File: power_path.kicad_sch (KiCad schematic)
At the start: 34 parts, among them J2 USB_C_Receptacle_USB2.0_16P, SW1 SW_SPST, U2 TPS631000DRLR, U3 TLV77018PDBVR, U4 TPS2116DRL, U5 USBLC6-2SC6, U6 USBLC6-2SC6, U8 BQ27427YZFR

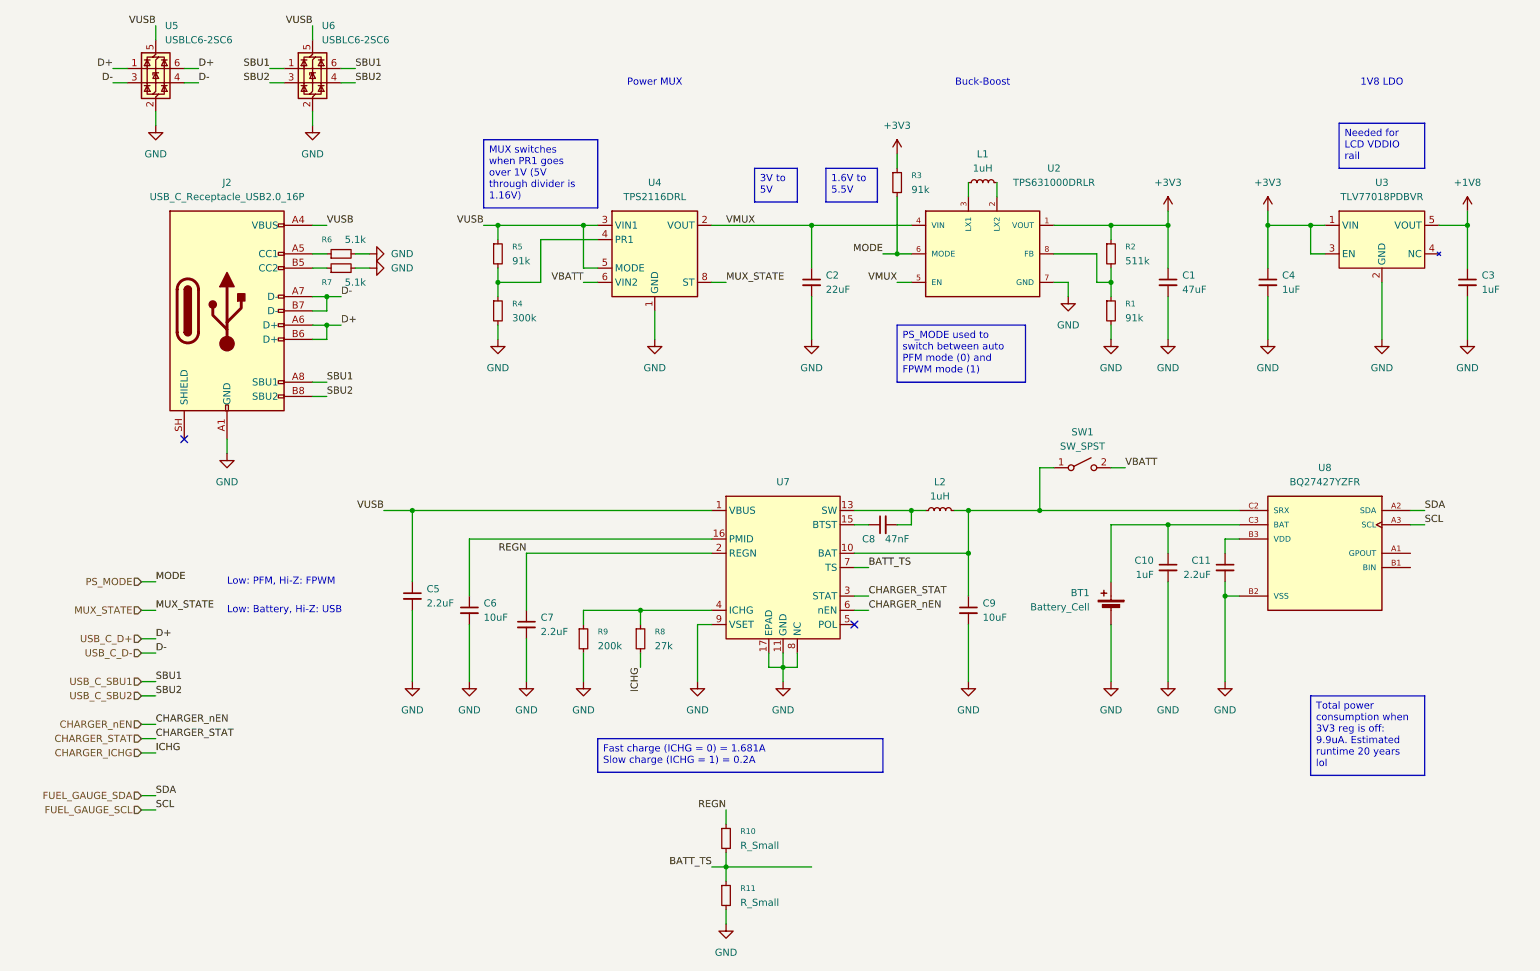
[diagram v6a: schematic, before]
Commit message: add pull up/down to fuel gauge
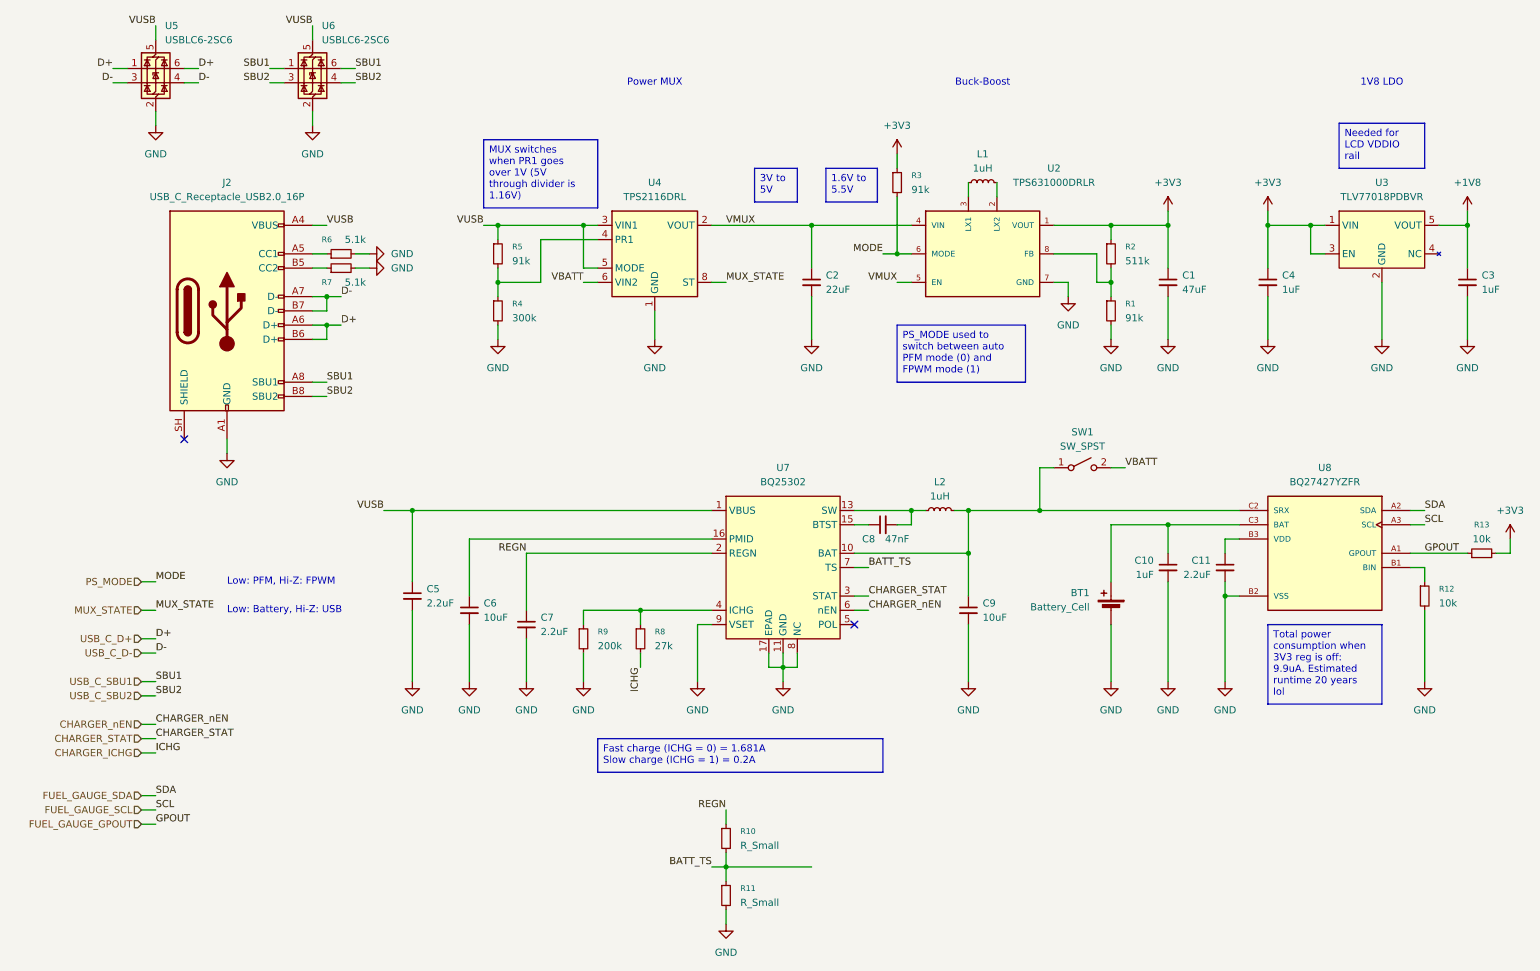
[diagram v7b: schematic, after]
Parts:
- added R12, R13: 10k, Resistor_SMD:R_0402_1005Metric, symbol Device:R_Small
- SW1: footprint (none) -> footprints:SK-12E12-G060
- U7: value (none) -> BQ25302
- U8: footprint BQ27427YZFR:IC_BQ27427YZFR -> footprints:IC_BQ27427YZFR
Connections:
- net +3V3: now also R13.2
- net GND: now also R12.2
- net FUEL_GAUGE_GPOUT: now reaches U8.A1 (GPOUT)
- net FUEL_GAUGE_GPOUT: now also R13.1
- net at U8.B1 (BIN): now also R12.1
- new net: SW1.3 (NC), SW1.M

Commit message: LDO NC pin to ground
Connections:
- net GND: now also U3.4 (NC)
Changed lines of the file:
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@@
+	(wire
+		(pts
+			(xy 266.7 68.58) (xy 266.7 83.82)
+		)
+		(stroke
+			(width 0)
+			(type default)
+		)
+	)
 	(wire
 		(pts
@@
 					(unit 1)
 				)
+			)
+		)
+	)
+	(symbol
+		(lib_id "power:GND")
+		(at 266.7 83.82 0)
+		(unit 1)
+		(body_style 1)
+		(exclude_from_sim no)
+		(in_bom yes)
+		(on_board yes)
+		(in_pos_files yes)
+		(dnp no)
+		(fields_autoplaced yes)
+		(property "Reference" "#PWR032"
+			(at 266.7 90.17 0)
+			(hide yes)
+			(show_name no)
+			(do_not_autoplace no)
+			(effects
+				(font
+					(size 1.27 1.27)
+				)
+			)
+		)
+		(property "Value" "GND"
+			(at 266.7 88.9 0)
+			(show_name no)
+			(do_not_autoplace no)
+			(effects
+				(font
+					(size 1.27 1.27)
+				)
+			)
+		)
+		(property "Footprint" ""
+			(at 266.7 83.82 0)
+			(hide yes)
+			(show_name no)
+			(do_not_autoplace no)
+			(effects
+				(font
+					(size 1.27 1.27)
+				)
+			)
+		)
+		(property "Datasheet" ""
+			(at 266.7 83.82 0)
+			(hide yes)
+			(show_name no)
+			(do_not_autoplace no)
+			(effects
+				(font
+					(size 1.27 1.27)
+				)
+			)
+		)
+		(property "Description" "Power symbol creates a global label with name \"GND\" , ground"
+			(at 266.7 83.82 0)
+			(hide yes)
+			(show_name no)
+			(do_not_autoplace no)
+			(effects
+				(font
+					(size 1.27 1.27)
+				)
+			)
+		)
+		(pin "1"
+		)
+		(instances
+			(project "pedal"
+				(path "/e2443317-b83f-4e66-ac79-3186c6d613f3/487ab5a8-1c1d-4a3e-8f62-a21afc38e9a3"
+					(reference "#PWR032")
+					(unit 1)
+				)
